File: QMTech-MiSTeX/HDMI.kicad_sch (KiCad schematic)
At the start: 33 parts, among them U1 ADV7513BSWZ, U2 TPS76318

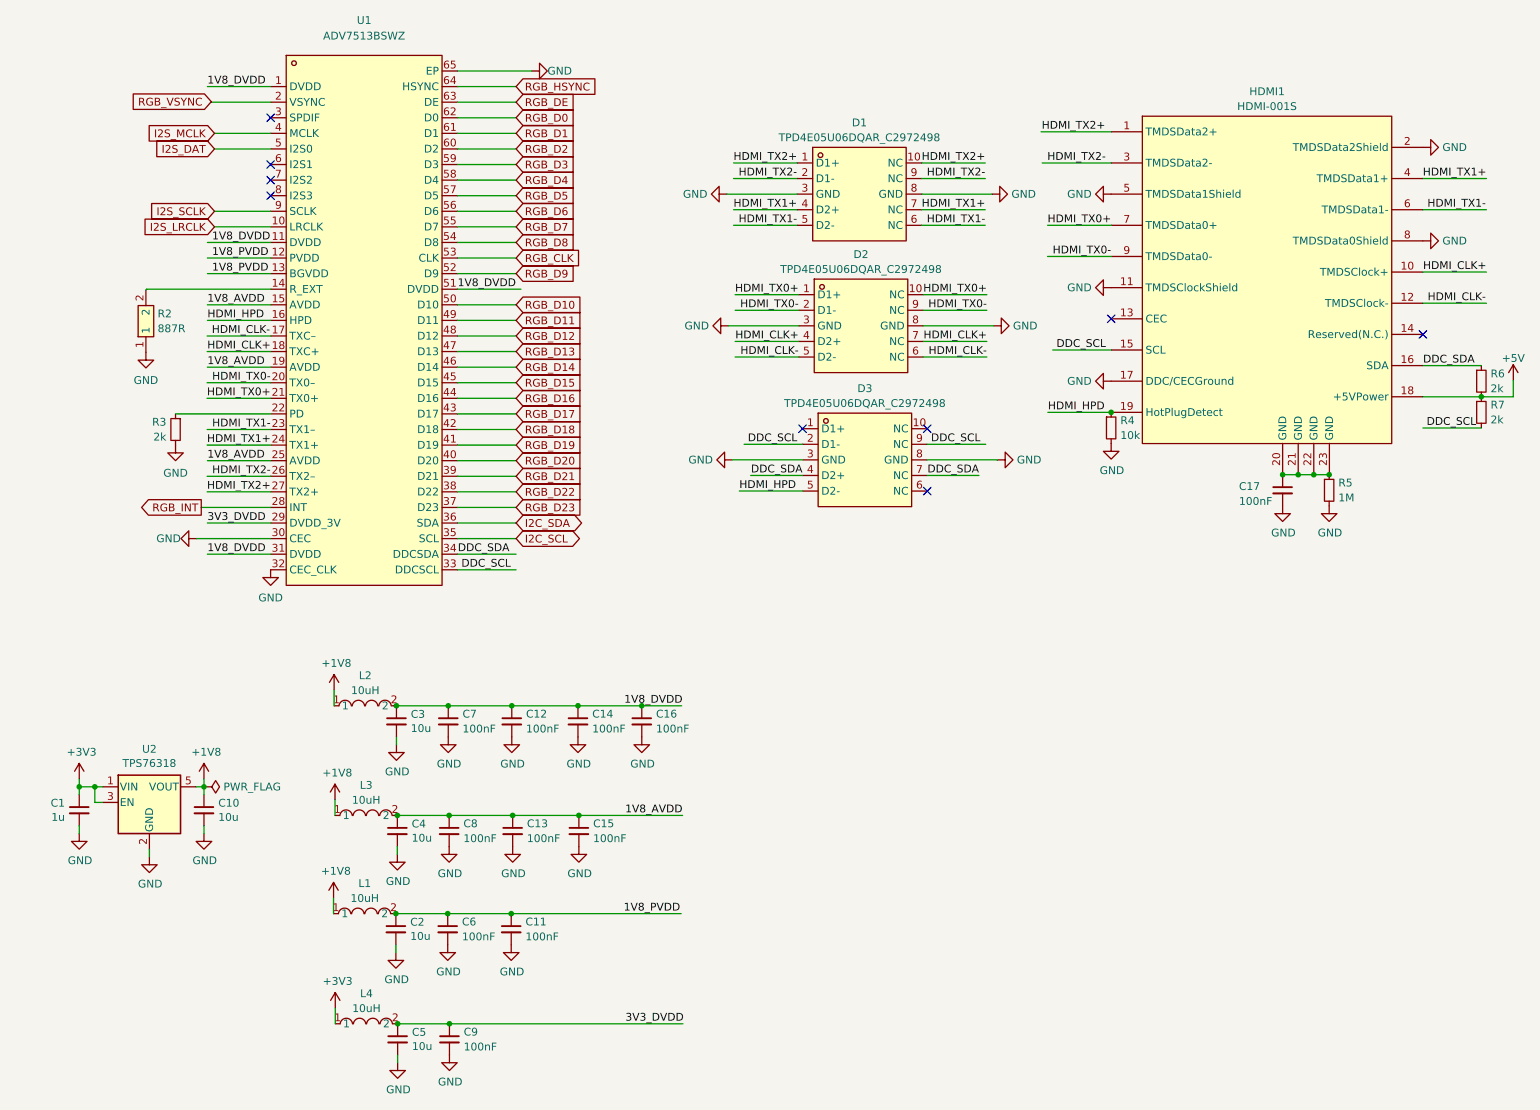
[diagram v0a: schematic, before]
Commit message: apply review notes from somhi, move audio into its own subsheet, add analog audio out
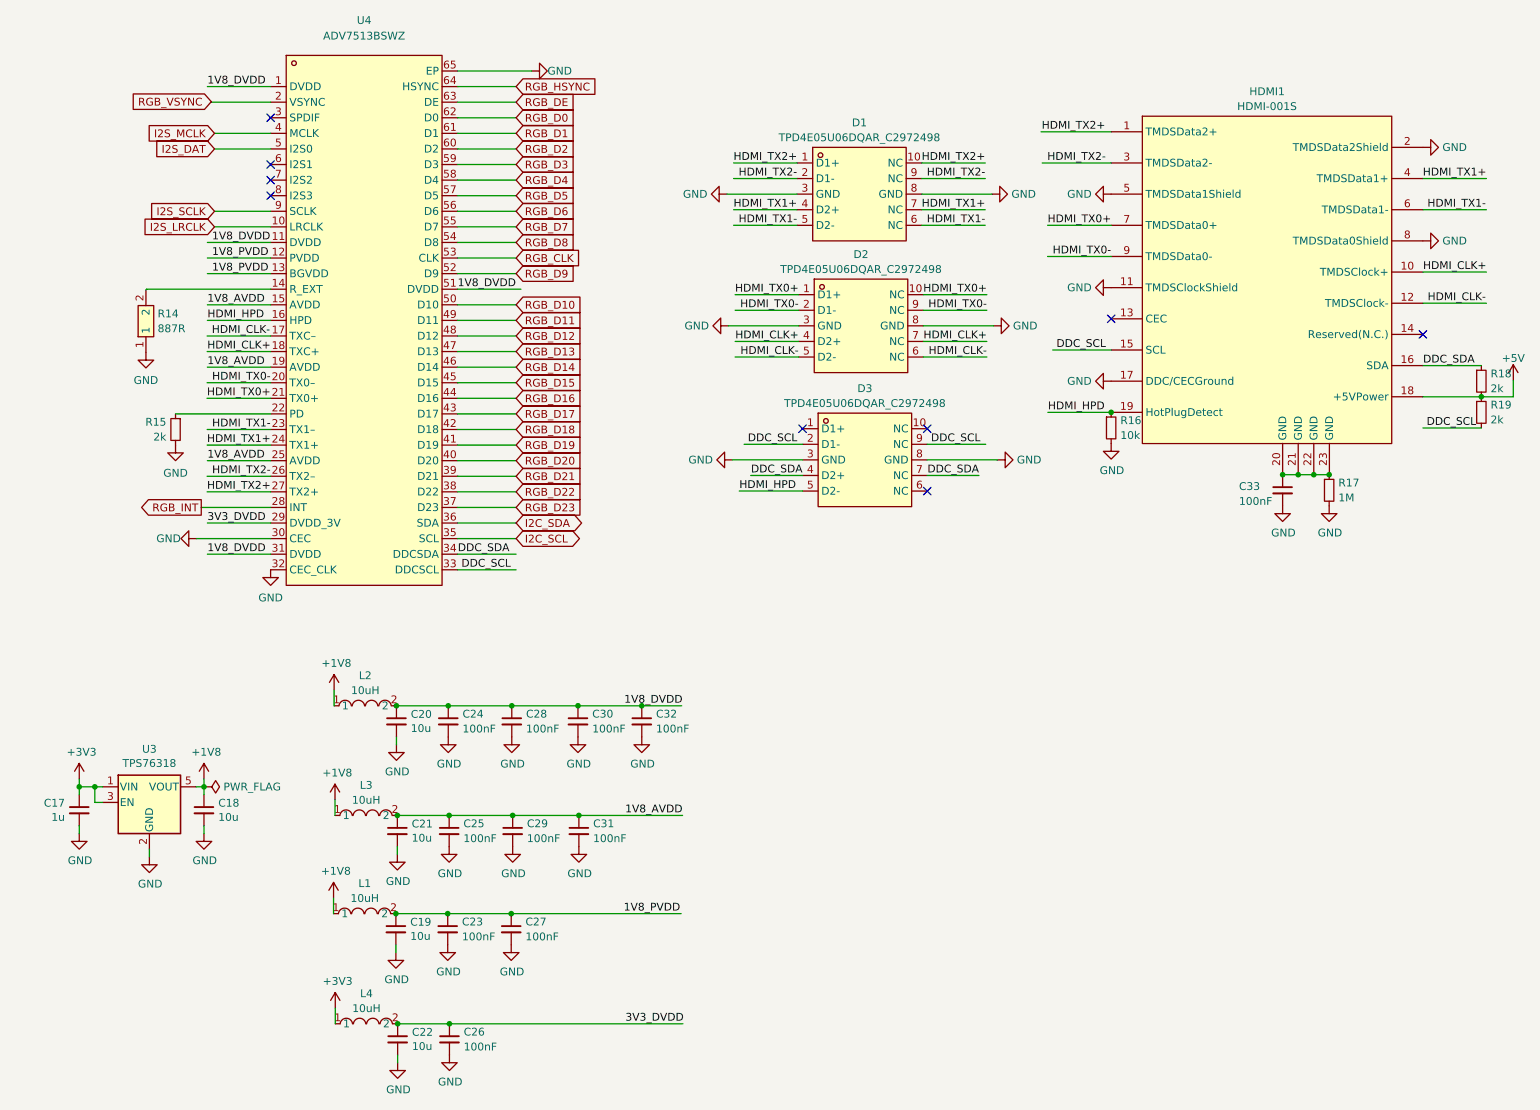
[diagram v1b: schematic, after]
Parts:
- renumbered C1 to C17, C10 to C18, C2 to C19, C3 to C20, C4 to C21, C5 to C22, C6 to C23, C7 to C24, C8 to C25, C9 to C26, C11 to C27, C12 to C28, C13 to C29, C14 to C30, C15 to C31, C16 to C32, C17 to C33, R2 to R14, R3 to R15, R4 to R16, R5 to R17, R6 to R18, R7 to R19, U2 to U3, U1 to U4

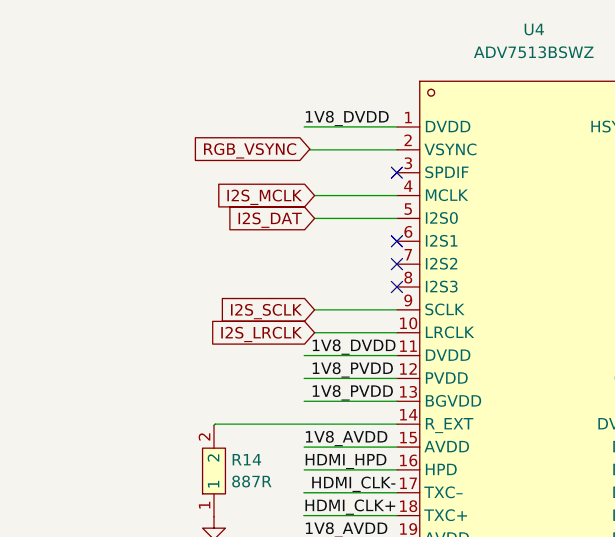
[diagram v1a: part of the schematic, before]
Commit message: QMTech-MiSTeX: make I2S audio to the DVI optional, use SPDIF by default
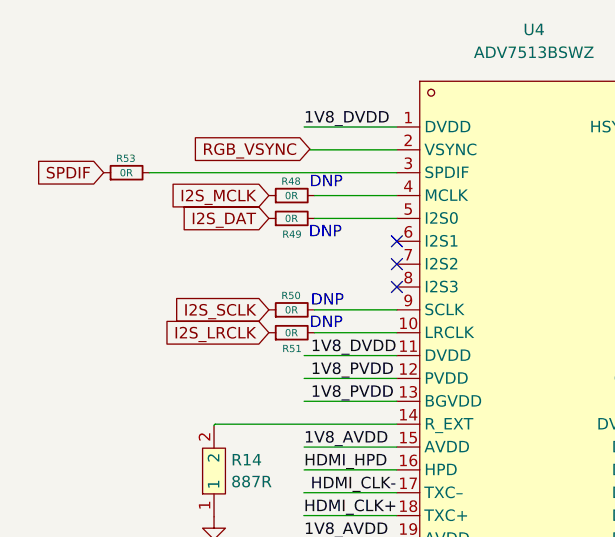
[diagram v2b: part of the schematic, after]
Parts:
- added R48, R49, R50, R51, R53: 0R, R_0402_1005Metric, symbol jlcpcb-basic-resistor-0402:0R
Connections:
- net I2S_DAT: now also R49.1; no longer U4.5 (I2S0)
- net I2S_LRCLK: now also R51.1; no longer U4.10 (LRCLK)
- net I2S_MCLK: now also R48.1; no longer U4.4 (MCLK)
- net I2S_SCLK: now also R50.1; no longer U4.9 (SCLK)
- net at U4.3 (SPDIF): now also R53.2
- new net: R49.2, U4.5 (I2S0)
- new net: R48.2, U4.4 (MCLK)
- new net: R51.2, U4.10 (LRCLK)
- new net: R50.2, U4.9 (SCLK)
- new net SPDIF: R53.1
- no-connect marks 9 -> 8
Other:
- note added: "DNP"
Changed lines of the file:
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@@
   (no_connect (at 196.2819 64.77))
   (no_connect (at 59.309 42.164))
-  (no_connect (at 59.309 32.004))
   (no_connect (at 166.3099 92.837))
   (no_connect (at 247.0819 67.31))
@@
     (stroke (width 0) (type default))
   )
+  (wire (pts (xy 26.7344 32.0016) (xy 26.7344 32.004))
+    (stroke (width 0) (type default))
+  )
   (wire (pts (xy 59.309 85.344) (xy 48.9619 85.344))
     (stroke (width 0) (type default))
@@
     (stroke (width 0) (type default))
   )
+  (wire (pts (xy 31.8144 32.004) (xy 59.309 32.004))
+    (stroke (width 0) (type default))
+  )
   (wire (pts (xy 49.0043 103.124) (xy 59.309 103.124))
     (stroke (width 0) (type default))
@@
     )
   )
+  (text "DNP" (at 49.5046 39.4716 0)
+    (effects (font (size 1.27 1.27)) (justify left bottom))
+  )
+  (text "DNP" (at 49.6062 49.5554 0)
+    (effects (font (size 1.27 1.27)) (justify left bottom))
+  )
+  (text "DNP" (at 49.6062 33.909 0)
+    (effects (font (size 1.27 1.27)) (justify left bottom))
+  )
+  (text "DNP" (at 49.7332 47.0662 0)
+    (effects (font (size 1.27 1.27)) (justify left bottom))
+  )
   (label "DDC_SCL" (at 195.426 69.85 180) (fields_autoplaced)
     (effects (font (size 1.27 1.27)) (justify right bottom))
@@
     )
   )
-  (global_label "I2S_DAT" (shape input) (at 50.165 37.084 180) (fields_autoplaced)
+  (global_label "SPDIF" (shape input) (at 26.7344 32.0016 180) (fields_autoplaced)
     (effects (font (size 1.27 1.27)) (justify right))
-    (property "Intersheetrefs" "${INTERSHEET_REFS}" (at 39.8622 37.084 0)
+    (property "Intersheetrefs" "${INTERSHEET_REFS}" (at 18.2112 32.0016 0)
+      (effects (font (size 1.27 1.27)) (justify right))
+    )
+  )
+  (global_label "I2S_DAT" (shape input) (at 45.085 37.084 180) (fields_autoplaced)
+    (effects (font (size 1.27 1.27)) (justify right))
+    (property "Intersheetrefs" "${INTERSHEET_REFS}" (at 34.7822 37.084 0)
       (effects (font (size 1.27 1.27)) (justify right))
     )
@@
     )
   )
-  (global_label "I2S_LRCLK" (shape input) (at 50.165 49.784 180) (fields_autoplaced)
+  (global_label "I2S_LRCLK" (shape input) (at 45.085 49.784 180) (fields_autoplaced)
     (effects (font (size 1.27 1.27)) (justify right))
-    (property "Intersheetrefs" "${INTERSHEET_REFS}" (at 37.3222 49.784 0)
+    (property "Intersheetrefs" "${INTERSHEET_REFS}" (at 32.2422 49.784 0)
       (effects (font (size 1.27 1.27)) (justify right))
     )
@@
     )
   )
-  (global_label "I2S_SCLK" (shape input) (at 50.165 47.244 180) (fields_autoplaced)
+  (global_label "I2S_SCLK" (shape input) (at 45.085 47.244 180) (fields_autoplaced)
     (effects (font (size 1.27 1.27)) (justify right))
-    (property "Intersheetrefs" "${INTERSHEET_REFS}" (at 38.4108 47.244 0)
+    (property "Intersheetrefs" "${INTERSHEET_REFS}" (at 33.3308 47.244 0)
       (effects (font (size 1.27 1.27)) (justify right))
     )
@@
     )
   )
-  (global_label "I2S_MCLK" (shape input) (at 50.165 34.544 180) (fields_autoplaced)
+  (global_label "I2S_MCLK" (shape input) (at 45.085 34.544 180) (fields_autoplaced)
     (effects (font (size 1.27 1.27)) (justify right))
-    (property "Intersheetrefs" "${INTERSHEET_REFS}" (at 38.1689 34.544 0)
+    (property "Intersheetrefs" "${INTERSHEET_REFS}" (at 33.0889 34.544 0)
       (effects (font (size 1.27 1.27)) (justify right))
     )
@@
     )
   )
+  (symbol (lib_id "jlcpcb-basic-resistor-0402:0R") (at 47.625 37.084 90) (unit 1)
+    (in_bom yes) (on_board yes) (dnp no)
+    (property "Reference" "R49" (at 47.6504 38.862 90)
+      (effects (font (size 0.8 0.8)))
+    )
+    (property "Value" "0R" (at 47.5996 37.1094 90)
+      (effects (font (size 0.8 0.8)))
+    )
+    (property "Footprint" "R_0402_1005Metric" (at 47.625 38.862 90)
+      (effects (font (size 1.27 1.27)) hide)
+    )
+    (property "Datasheet" "https://datasheet.lcsc.com/szlcsc/Uniroyal-Elec-0402WGF0000TCE_C17168.pdf" (at 47.625 37.084 90)
+      (effects (font (size 1.27 1.27)) hide)
+    )
+    (pin "1")
+    (pin "2")
+    (instances
+      (project "QMTech-MiSTeX"
+        (path "/bf95850e-2fcb-4784-a603-f17fc357556b/5d48eec1-381e-4cbb-abac-13dba509fc03"
+          (reference "R49") (unit 1)
+        )
+      )
+    )
+  )
   (symbol (lib_id "power:+1V8") (at 48.4447 139.7647 0) (unit 1)
     (in_bom yes) (on_board yes) (dnp no)
@@
     )
   )
+  (symbol (lib_id "jlcpcb-basic-resistor-0402:0R") (at 47.625 34.544 90) (unit 1)
+    (in_bom yes) (on_board yes) (dnp no)
+    (property "Reference" "R48" (at 47.5488 32.9692 90)
+      (effects (font (size 0.8 0.8)))
+    )
+    (property "Value" "0R" (at 47.5996 34.5694 90)
+      (effects (font (size 0.8 0.8)))
+    )
+    (property "Footprint" "R_0402_1005Metric" (at 47.625 36.322 90)
+      (effects (font (size 1.27 1.27)) hide)
+    )
+    (property "Datasheet" "https://datasheet.lcsc.com/szlcsc/Uniroyal-Elec-0402WGF0000TCE_C17168.pdf" (at 47.625 34.544 90)
+      (effects (font (size 1.27 1.27)) hide)
+    )
+    (pin "1")
+    (pin "2")
+    (instances
+      (project "QMTech-MiSTeX"
+        (path "/bf95850e-2fcb-4784-a603-f17fc357556b/5d48eec1-381e-4cbb-abac-13dba509fc03"
+          (reference "R48") (unit 1)
+        )
+      )
+    )
+  )
   (symbol (lib_id "easyeda2kicad:SDFL2012S100KTF") (at 74.6439 161.6987 0) (unit 1)
     (in_bom yes) (on_board yes) (dnp no) (fields_autoplaced)
@@
     )
   )
+  (symbol (lib_id "jlcpcb-basic-resistor-0402:0R") (at 29.2744 32.004 90) (unit 1)
+    (in_bom yes) (on_board yes) (dnp no)
+    (property "Reference" "R53" (at 29.1982 30.4292 90)
+      (effects (font (size 0.8 0.8)))
+    )
+    (property "Value" "0R" (at 29.249 32.0294 90)
+      (effects (font (size 0.8 0.8)))
+    )
+    (property "Footprint" "R_0402_1005Metric" (at 29.2744 33.782 90)
+      (effects (font (size 1.27 1.27)) hide)
+    )
+    (property "Datasheet" "https://datasheet.lcsc.com/szlcsc/Uniroyal-Elec-0402WGF0000TCE_C17168.pdf" (at 29.2744 32.004 90)
+      (effects (font (size 1.27 1.27)) hide)
+    )
+    (property "LCSC" "C17168" (at 29.2744 32.004 90)
+      (effects (font (size 1.27 1.27)) hide)
+    )
+    (pin "1")
+    (pin "2")
+    (instances
+      (project "QMTech-MiSTeX"
+        (path "/bf95850e-2fcb-4784-a603-f17fc357556b/5d48eec1-381e-4cbb-abac-13dba509fc03"
+          (reference "R53") (unit 1)
+        )
+      )
+    )
+  )
   (symbol (lib_id "power:GND") (at 80.0066 185.9927 0) (unit 1)
     (in_bom yes) (on_board yes) (dnp no)
@@
     )
   )
+  (symbol (lib_id "jlcpcb-basic-resistor-0402:0R") (at 47.625 49.784 90) (unit 1)
+    (in_bom yes) (on_board yes) (dnp no)
+    (property "Reference" "R51" (at 47.6504 51.562 90)
+      (effects (font (size 0.8 0.8)))
+    )
+    (property "Value" "0R" (at 47.5996 49.8094 90)
+      (effects (font (size 0.8 0.8)))
+    )
+    (property "Footprint" "R_0402_1005Metric" (at 47.625 51.562 90)
+      (effects (font (size 1.27 1.27)) hide)
+    )
+    (property "Datasheet" "https://datasheet.lcsc.com/szlcsc/Uniroyal-Elec-0402WGF0000TCE_C17168.pdf" (at 47.625 49.784 90)
+      (effects (font (size 1.27 1.27)) hide)
+    )
+    (pin "1")
+    (pin "2")
+    (instances
+      (project "QMTech-MiSTeX"
+        (path "/bf95850e-2fcb-4784-a603-f17fc357556b/5d48eec1-381e-4cbb-abac-13dba509fc03"
+          (reference "R51") (unit 1)
+        )
+      )
+    )
+  )
   (symbol (lib_id "power:GND") (at 134.5599 87.757 270) (mirror x) (unit 1)
     (in_bom yes) (on_board yes) (dnp no) (fields_autoplaced)
@@
         )
       )
+    )
+  )
+  (symbol (lib_id "jlcpcb-basic-resistor-0402:0R") (at 47.625 47.244 90) (unit 1)
+    (in_bom yes) (on_board yes) (dnp no)
+    (property "Reference" "R50" (at 47.5488 45.6692 90)
+      (effects (font (size 0.8 0.8)))
+    )
+    (property "Value" "0R" (at 47.5996 47.2694 90)
+      (effects (font (size 0.8 0.8)))
+    )
+    (property "Footprint" "R_0402_1005Metric" (at 47.625 49.022 90)
+      (effects (font (size 1.27 1.27)) hide)
+    )
+    (property "Datasheet" "https://datasheet.lcsc.com/szlcsc/Uniroyal-Elec-0402WGF0000TCE_C17168.pdf" (at 47.625 47.244 90)
+      (effects (font (size 1.27 1.27)) hide)
+    )
+    (pin "1")
+    (pin "2")
+    (instances
+      (project "QMTech-MiSTeX"
+        (path "/bf95850e-2fcb-4784-a603-f17fc357556b/5d48eec1-381e-4cbb-abac-13dba509fc03"
+          (reference "R50") (unit 1)
+        )
+      )
